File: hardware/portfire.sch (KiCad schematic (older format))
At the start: 70 parts, among them P101 1, P102 11, P103 2, P104 12, P105 3, P106 13, P107 4, P108 14, P109 5, P110 15, P111 6, P112 21, P113 7, P114 22, P115 8, P116 23, P117 9, P118 24, P119 10, P120 25, P121 16, P122 17, P123 18, P124 19, P125 20, P126 26, P127 27, P128 28, P129 29, P130 30

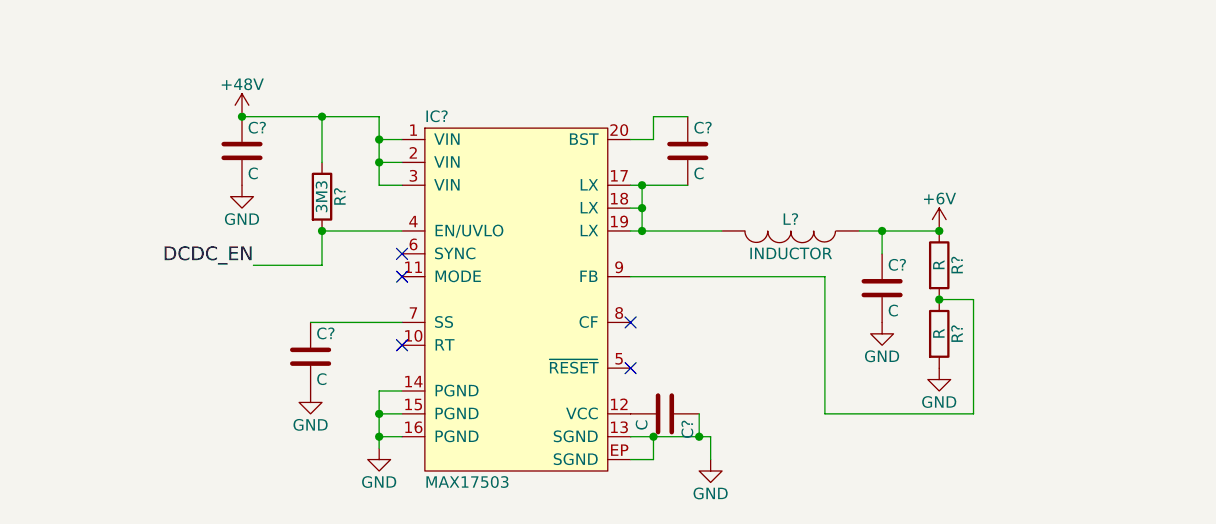
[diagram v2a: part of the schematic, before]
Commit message: SMPS schematic design
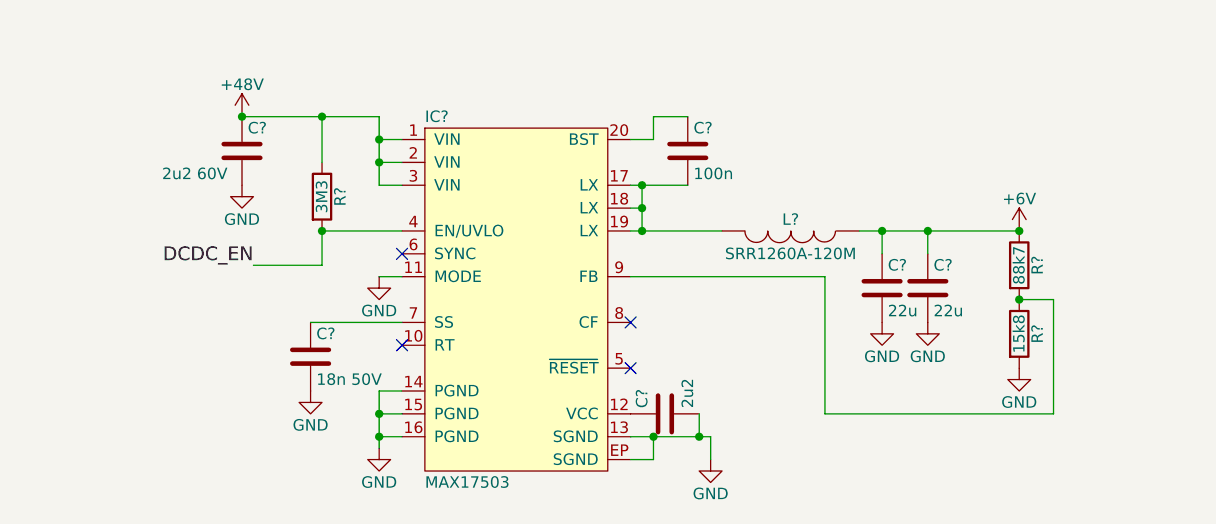
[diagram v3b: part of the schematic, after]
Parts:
- added C?: 22u, agg-kicad:1206, symbol C
- C?: value C -> 2u2 60V; footprint (none) -> agg-kicad:1210; Farnell (none) -> 1793832
- C?: value C -> 2u2; footprint (none) -> agg-kicad:0603; Farnell (none) -> 2496923
- C?: value C -> 18n 50V; footprint (none) -> agg-kicad:0603; Farnell (none) -> 1865536
- C?: value C -> 100n; footprint (none) -> agg-kicad:0603; Farnell (none) -> 1650835
- C?: value C -> 22u; footprint (none) -> agg-kicad:1206; Farnell (none) -> 2118135
- L?: value INDUCTOR -> SRR1260A-120M; Farnell (none) -> 2374123
- R?: value R -> 88k7; footprint (none) -> agg-kicad:0603; Farnell (none) -> 2059491
- R?: value R -> 15k8; footprint (none) -> agg-kicad:0603; Farnell (none) -> 2138432
- R?: footprint (none) -> agg-kicad:0603; Farnell (none) -> 2138666
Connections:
- net +6V: now also C?.1
- net GND: now also C?.2, IC?.11 (MODE), C?.2; no longer C?.1
- net at IC?.12 (VCC): now also C?.1; no longer C?.2
- no-connect marks 6 -> 5
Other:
- moved on the sheet: R?
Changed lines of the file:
@@
 P 1850 5950
 F 0 "C?" H 1875 6050 50  0000 L CNN
-F 1 "C" H 1875 5850 50  0000 L CNN
-F 2 "" H 1888 5800 50  0000 C CNN
+F 1 "2u2 60V" H 1500 5850 50  0000 L CNN
+F 2 "agg-kicad:1210" H 1888 5800 50  0001 C CNN
 F 3 "" H 1850 5950 50  0000 C CNN
+F 4 "1793832" H 1850 5950 60  0001 C CNN "Farnell"
 	1    1850 5950
 	1    0    0    -1
@@
 P 3700 7100
 F 0 "C?" H 3725 7200 50  0000 L CNN
-F 1 "C" H 3725 7000 50  0000 L CNN
-F 2 "" H 3738 6950 50  0000 C CNN
+F 1 "2u2" H 3725 7000 50  0000 L CNN
+F 2 "agg-kicad:0603" H 3738 6950 50  0001 C CNN
 F 3 "" H 3700 7100 50  0000 C CNN
+F 4 "2496923" H 3700 7100 60  0001 C CNN "Farnell"
 	1    3700 7100
-	0    1    1    0
+	0    -1   -1   0
 $EndComp
 $Comp
@@
 P 2150 6850
 F 0 "C?" H 2175 6950 50  0000 L CNN
-F 1 "C" H 2175 6750 50  0000 L CNN
-F 2 "" H 2188 6700 50  0000 C CNN
-F 3 "" H 2150 6850 50  0000 C CNN
+F 1 "18n 50V" H 2175 6750 50  0000 L CNN
+F 2 "agg-kicad:0603" H 2188 6700 50  0001 C CNN
+F 3 "http://www.farnell.com/datasheets/2120276.pdf" H 2150 6850 50  0001 C CNN
+F 4 "1865536" H 2150 6850 60  0001 C CNN "Farnell"
 	1    2150 6850
 	1    0    0    -1
@@
 P 3800 5950
 F 0 "C?" H 3825 6050 50  0000 L CNN
-F 1 "C" H 3825 5850 50  0000 L CNN
-F 2 "" H 3838 5800 50  0000 C CNN
+F 1 "100n" H 3825 5850 50  0000 L CNN
+F 2 "agg-kicad:0603" H 3838 5800 50  0001 C CNN
 F 3 "" H 3800 5950 50  0000 C CNN
+F 4 "1650835" H 3800 5950 60  0001 C CNN "Farnell"
 	1    3800 5950
 	1    0    0    -1
@@
 P 4250 6300
 F 0 "L?" V 4200 6300 50  0000 C CNN
-F 1 "INDUCTOR" V 4350 6300 50  0000 C CNN
-F 2 "" H 4250 6300 50  0000 C CNN
-F 3 "" H 4250 6300 50  0000 C CNN
+F 1 "SRR1260A-120M" V 4350 6300 50  0000 C CNN
+F 2 "" H 4250 6300 50  0001 C CNN
+F 3 "http://www.farnell.com/datasheets/2059617.pdf" H 4250 6300 50  0001 C CNN
+F 4 "2374123" H 4250 6300 60  0001 C CNN "Farnell"
 	1    4250 6300
 	0    1    1    0
@@
 P 4650 6550
 F 0 "C?" H 4675 6650 50  0000 L CNN
-F 1 "C" H 4675 6450 50  0000 L CNN
-F 2 "" H 4688 6400 50  0000 C CNN
-F 3 "" H 4650 6550 50  0000 C CNN
+F 1 "22u" H 4675 6450 50  0000 L CNN
+F 2 "agg-kicad:1206" H 4688 6400 50  0001 C CNN
+F 3 "http://www.farnell.com/datasheets/2120596.pdf" H 4650 6550 50  0001 C CNN
+F 4 "2118135" H 4650 6550 60  0001 C CNN "Farnell"
 	1    4650 6550
 	1    0    0    -1
@@
 L +6V #PWR?
 U 1 1 57E8960A
-P 4900 6300
-F 0 "#PWR?" H 4900 6150 50  0001 C CNN
-F 1 "+6V" H 4900 6440 50  0000 C CNN
-F 2 "" H 4900 6300 50  0000 C CNN
-F 3 "" H 4900 6300 50  0000 C CNN
-	1    4900 6300
+P 5250 6300
+F 0 "#PWR?" H 5250 6150 50  0001 C CNN
+F 1 "+6V" H 5250 6440 50  0000 C CNN
+F 2 "" H 5250 6300 50  0000 C CNN
+F 3 "" H 5250 6300 50  0000 C CNN
+	1    5250 6300
 	1    0    0    -1
 $EndComp
@@
 L R R?
 U 1 1 57E89692
-P 4900 6450
-F 0 "R?" V 4980 6450 50  0000 C CNN
-F 1 "R" V 4900 6450 50  0000 C CNN
-F 2 "" V 4830 6450 50  0000 C CNN
-F 3 "" H 4900 6450 50  0000 C CNN
-	1    4900 6450
+P 5250 6450
+F 0 "R?" V 5330 6450 50  0000 C CNN
+F 1 "88k7" V 5250 6450 50  0000 C CNN
+F 2 "agg-kicad:0603" V 5180 6450 50  0001 C CNN
+F 3 "http://www.farnell.com/datasheets/1911175.pdf" H 5250 6450 50  0001 C CNN
+F 4 "2059491" H 5250 6450 60  0001 C CNN "Farnell"
+	1    5250 6450
 	1    0    0    -1
 $EndComp
@@
 L R R?
 U 1 1 57E89729
-P 4900 6750
-F 0 "R?" V 4980 6750 50  0000 C CNN
-F 1 "R" V 4900 6750 50  0000 C CNN
-F 2 "" V 4830 6750 50  0000 C CNN
-F 3 "" H 4900 6750 50  0000 C CNN
-	1    4900 6750
+P 5250 6750
+F 0 "R?" V 5330 6750 50  0000 C CNN
+F 1 "15k8" V 5250 6750 50  0000 C CNN
+F 2 "agg-kicad:0603" V 5180 6750 50  0001 C CNN
+F 3 "http://www.farnell.com/datasheets/2111203.pdf" H 5250 6750 50  0001 C CNN
+F 4 "2138432" H 5250 6750 60  0001 C CNN "Farnell"
+	1    5250 6750
 	1    0    0    -1
 $EndComp
@@
 L GND #PWR?
 U 1 1 57E897BB
-P 4900 6900
-F 0 "#PWR?" H 4900 6650 50  0001 C CNN
-F 1 "GND" H 4900 6750 50  0000 C CNN
-F 2 "" H 4900 6900 50  0000 C CNN
-F 3 "" H 4900 6900 50  0000 C CNN
-	1    4900 6900
+P 5250 6900
+F 0 "#PWR?" H 5250 6650 50  0001 C CNN
+F 1 "GND" H 5250 6750 50  0000 C CNN
+F 2 "" H 5250 6900 50  0000 C CNN
+F 3 "" H 5250 6900 50  0000 C CNN
+	1    5250 6900
 	1    0    0    -1
 $EndComp
 NoConn ~ 2550 6400
 NoConn ~ 2550 6800
-NoConn ~ 2550 6500
 NoConn ~ 3550 6900
 Wire Wire Line
@@
 Connection ~ 3600 6300
 Wire Wire Line
-	4550 6300 4900 6300
+	4550 6300 5250 6300
 Wire Wire Line
 	4650 6300 4650 6400
 Connection ~ 4650 6300
-Connection ~ 4900 6300
-Connection ~ 4900 6600
-Wire Wire Line
-	4900 6600 5050 6600
-Wire Wire Line
-	5050 6600 5050 7100
-Wire Wire Line
-	5050 7100 4400 7100
+Connection ~ 5250 6300
+Connection ~ 5250 6600
+Wire Wire Line
+	5250 6600 5400 6600
+Wire Wire Line
+	5400 6600 5400 7100
+Wire Wire Line
+	5400 7100 4400 7100
 Wire Wire Line
 	4400 7100 4400 6500
@@
 F 0 "R?" V 2280 6150 50  0000 C CNN
 F 1 "3M3" V 2200 6150 50  0000 C CNN
-F 2 "" V 2130 6150 50  0000 C CNN
+F 2 "agg-kicad:0603" V 2130 6150 50  0001 C CNN
 F 3 "" H 2200 6150 50  0000 C CNN
+F 4 "2138666" H 2200 6150 60  0001 C CNN "Farnell"
 	1    2200 6150
 	1    0    0    -1
@@
 	1    0    0    -1
 $EndComp
+$Comp
+L C C?
+U 1 1 57F02E4B
+P 4850 6550
+F 0 "C?" H 4875 6650 50  0000 L CNN
+F 1 "22u" H 4875 6450 50  0000 L CNN
+F 2 "agg-kicad:1206" H 4888 6400 50  0001 C CNN
+F 3 "http://www.farnell.com/datasheets/2120596.pdf" H 4850 6550 50  0001 C CNN
+F 4 "2118135" H 4850 6550 60  0001 C CNN "Farnell"
+	1    4850 6550
+	1    0    0    -1
+$EndComp
+Wire Wire Line
+	4850 6300 4850 6400
+Connection ~ 4850 6300
+$Comp
+L GND #PWR?
+U 1 1 57F031F8
+P 4850 6700
+F 0 "#PWR?" H 4850 6450 50  0001 C CNN
+F 1 "GND" H 4850 6550 50  0000 C CNN
+F 2 "" H 4850 6700 50  0000 C CNN
+F 3 "" H 4850 6700 50  0000 C CNN
+	1    4850 6700
+	1    0    0    -1
+$EndComp
+$Comp
+L GND #PWR?
+U 1 1 57F07292
+P 2450 6500
+F 0 "#PWR?" H 2450 6250 50  0001 C CNN
+F 1 "GND" H 2450 6350 50  0000 C CNN
+F 2 "" H 2450 6500 50  0000 C CNN
+F 3 "" H 2450 6500 50  0000 C CNN
+	1    2450 6500
+	1    0    0    -1
+$EndComp
+Wire Wire Line
+	2450 6500 2550 6500
 $EndSCHEMATC

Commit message: Added SMPS inductor footprint
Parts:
- L?: footprint (none) -> hardware:SRR1260A
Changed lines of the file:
@@
 F 0 "L?" V 4200 6300 50  0000 C CNN
 F 1 "SRR1260A-120M" V 4350 6300 50  0000 C CNN
-F 2 "" H 4250 6300 50  0001 C CNN
+F 2 "hardware:SRR1260A" H 4250 6300 50  0001 C CNN
 F 3 "http://www.farnell.com/datasheets/2059617.pdf" H 4250 6300 50  0001 C CNN
 F 4 "2374123" H 4250 6300 60  0001 C CNN "Farnell"

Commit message: Fixed fp references
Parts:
- removed C? (x3): 10n 200V, agg-kicad:0805, symbol C
- removed D? (x7): SS110B, agg-kicad:DO-214AA-SMB, symbol D_Small
- removed R? (x3): 75, agg-kicad:0603, symbol R
- added C4, C6, C7: 10n 200V, agg:0805, symbol C
- added D2, D3, D4, D5, D6, D7, D8: SS110B, agg:DO-214AA-SMB, symbol D_Small
- added R2, R4, R5: 75, agg:0603, symbol R
- C1: renamed from C?; footprint agg-kicad:1210 -> agg:1210
- C10, C11, C12, C3, C9: renamed from C?; footprint agg-kicad:0603 -> agg:0603
- C13, C14, C5: renamed from C?; footprint agg-kicad:1206 -> agg:1206
- C2, C8: renamed from C?; footprint agg-kicad:0805 -> agg:0805
- D1: renamed from D?; footprint agg-kicad:DO-214AA-SMB -> agg:DO-214AA-SMB
- D9: renamed from D?; footprint agg-kicad:DO-214AC-SMA -> agg:DO-214AC-SMA
- R1, R3, R6, R7, R8, R9: renamed from R?; footprint agg-kicad:0603 -> agg:0603
- gave numbers to parts that had none: 9
- renumbered P101 to P1, P119 to P10, P102 to P11, P104 to P12, P106 to P13, P108 to P14, P110 to P15, P121 to P16, P122 to P17, P123 to P18, P124 to P19, P103 to P2, P125 to P20, P112 to P21, P114 to P22, P116 to P23, P118 to P24, P120 to P25, P126 to P26, P127 to P27, P128 to P28, P129 to P29, P105 to P3, P130 to P30, P107 to P4, P109 to P5, P111 to P6, P113 to P7, P115 to P8, P117 to P9
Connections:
- net VA1: now also C6.1, D2.1 (K)
- net VA2: now also C7.1, D3.2 (A), D4.1 (K)
- net VB1: now also D5.2 (A), D6.1 (K)
- net VB2: now also C4.1, D7.2 (A), D8.1 (K)
- net at C8.1, D1.1 (K), D9.1 (K)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: now also D3.1 (K), D5.1 (K), D7.1 (K)
- net at C8.2, D9.2 (A), IC2.5 (VSS)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: now also D2.2 (A), D4.2 (A), D6.2 (A), D8.2 (A)
- net at C5.1, R1.2: now also R2.2, R4.2, R5.2
- new net: C4.2, R2.1
- new net: C6.2, R4.1
- new net: C7.2, R5.1

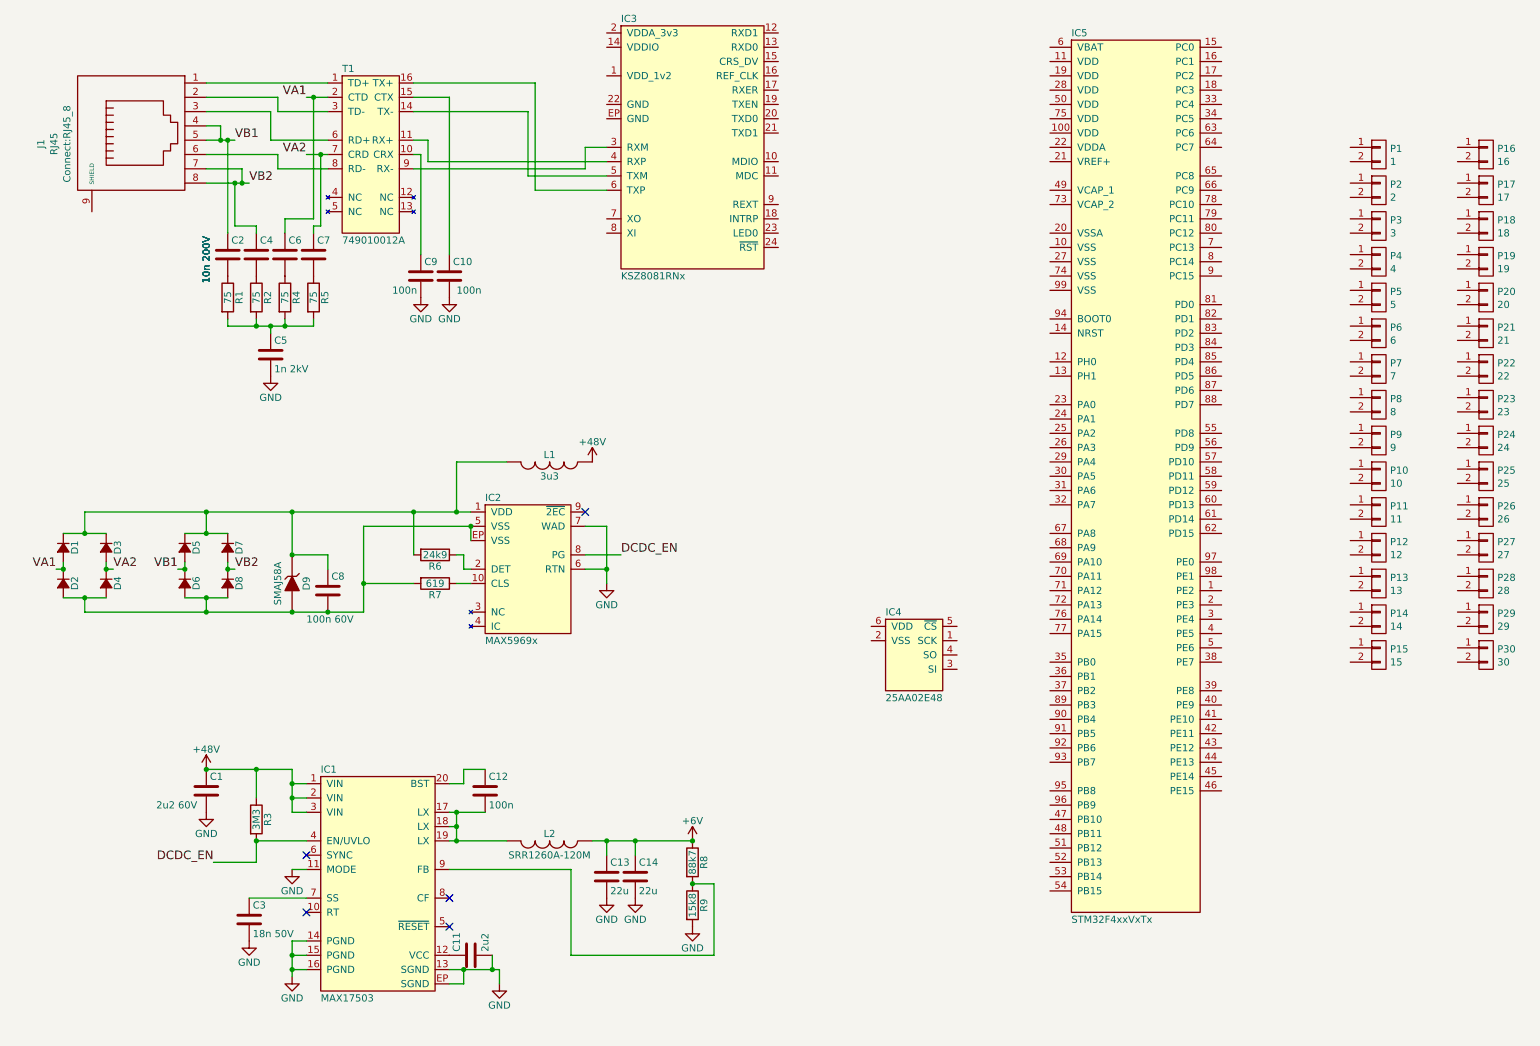
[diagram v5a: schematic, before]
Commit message: Hierarchical sheets, connected up RMII/PD pins
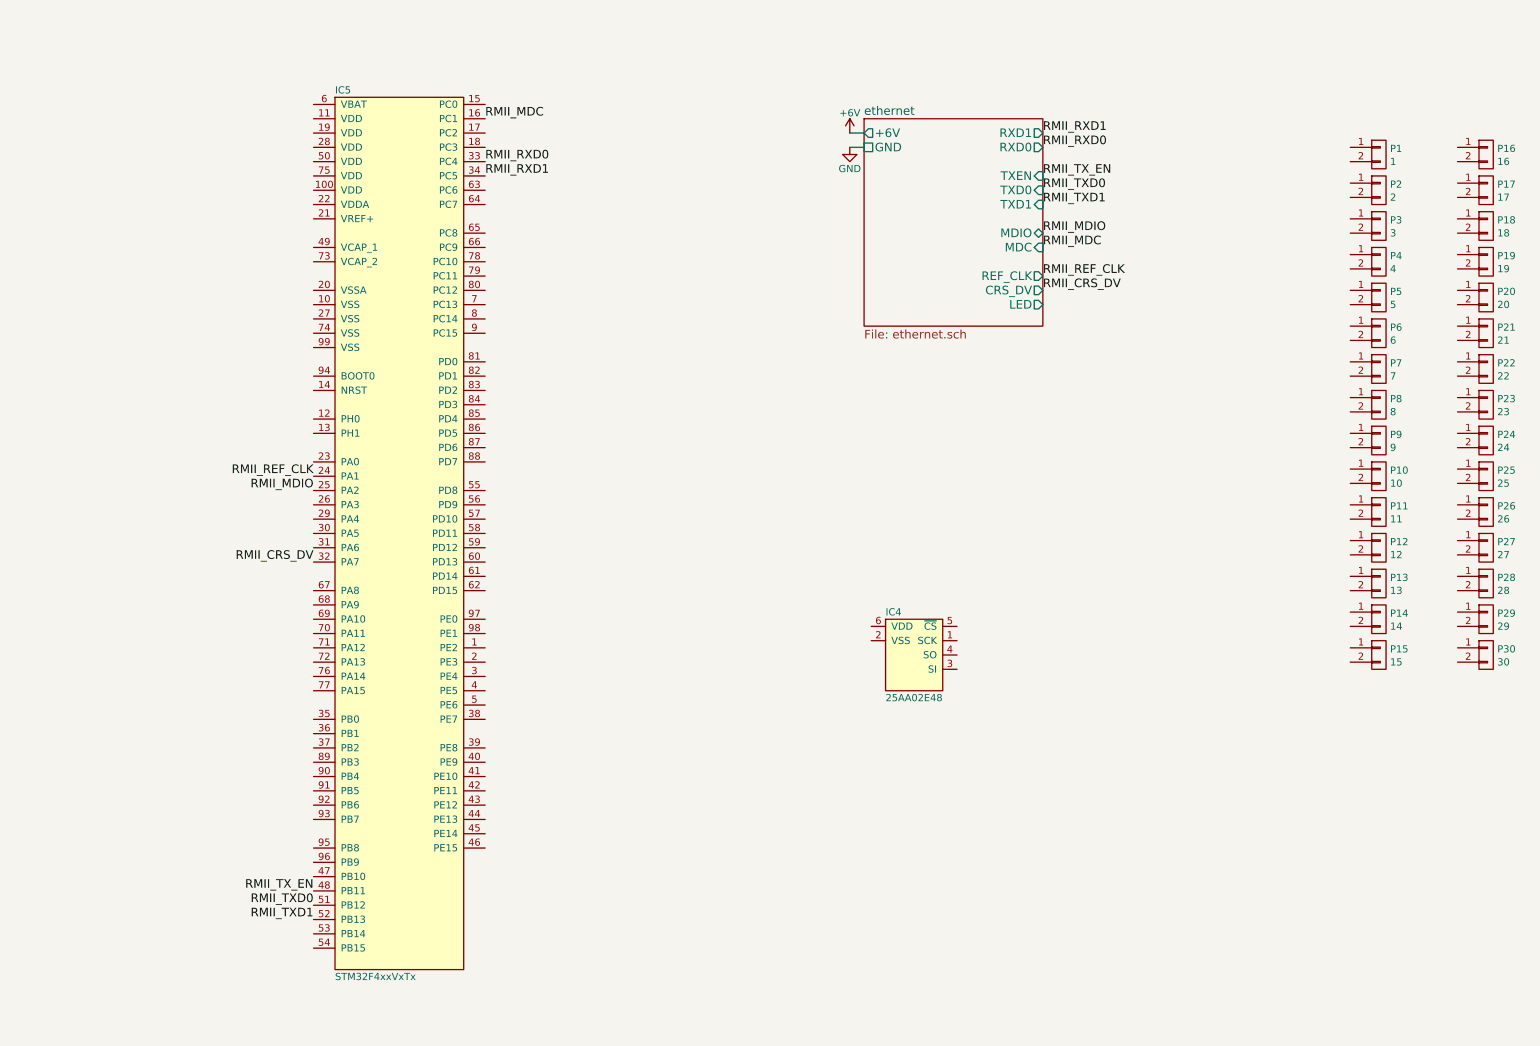
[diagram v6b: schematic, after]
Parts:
- removed C1: 2u2 60V, agg:1210, symbol C
- removed C10, C12, C9: 100n, agg:0603, symbol C
- removed C11: 2u2, agg:0603, symbol C
- removed C13, C14: 22u, agg:1206, symbol C
- removed C2, C4, C6, C7: 10n 200V, agg:0805, symbol C
- removed C3: 18n 50V, agg:0603, symbol C
- removed C5: 1n 2kV, agg:1206, symbol C
- removed C8: 100n 60V, agg:0805, symbol C
- removed D1, D2, D3, D4, D5, D6, D7, D8: SS110B, agg:DO-214AA-SMB, symbol D_Small
- removed D9: SMAJ58A, agg:DO-214AC-SMA, symbol ZENER
- removed IC1: MAX17503, agg:QFN-20-EP-MAX, symbol MAX17503
- removed IC2: MAX5969x, agg:DFN-10-EP-MAX, symbol MAX5969x
- removed IC3: KSZ8081RNx, agg:QFN-24-EP-MICREL, symbol KSZ8081RNx
- removed J1: RJ45, Connect:RJ45_8, symbol RJ45
- removed L1: 3u3, hardware:ELLATP3R3NB, symbol INDUCTOR
- removed L2: SRR1260A-120M, hardware:SRR1260A, symbol INDUCTOR
- removed R1, R2, R4, R5: 75, agg:0603, symbol R
- removed R3: 3M3, agg:0603, symbol R
- removed R6: 24k9, agg:0603, symbol R
- removed R7: 619, agg:0603, symbol R
- removed R8: 88k7, agg:0603, symbol R
- removed R9: 15k8, agg:0603, symbol R
- removed T1: 749010012A, agg:749010012A, symbol 749010012A
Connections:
- net RMII_MDC: now reaches IC5.16 (PC1)
- net RMII_REF_CLK: now reaches IC5.24 (PA1)
- net RMII_MDIO: now reaches IC5.25 (PA2)
- net RMII_CRS_DV: now reaches IC5.32 (PA7)
- net RMII_RXD0: now reaches IC5.33 (PC4)
- net RMII_RXD1: now reaches IC5.34 (PC5)
- net RMII_TX_EN: now reaches IC5.48 (PB11)
- net RMII_TXD0: now reaches IC5.51 (PB12)
- net RMII_TXD1: now reaches IC5.52 (PB13)
- no-connect marks 5 -> 0
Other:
- moved on the sheet: IC5
